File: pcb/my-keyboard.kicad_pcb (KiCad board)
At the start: 2 copper layers, 8 parts, among them J1 Conn_01x04_Socket, SW1 SW_Push, SW2 SW_Push, SW3 SW_Push, SW4 SW_Push, SW5 RotaryEncoder_Switch, SW6 RotaryEncoder_Switch, U1 MOUDLE-SEEEDUINO-XIAO

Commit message: New PCB and gerber files
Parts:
- added H1: MountingHole, MountingHole:MountingHole_3.5mm, F.Cu at (167.0, 98.5)
- added H2: MountingHole, MountingHole:MountingHole_3.5mm, F.Cu at (105.5, 65.0)
- added H3: MountingHole, MountingHole:MountingHole_3.5mm, F.Cu at (102.5, 104.0)
- moved SW5 0.56 mm to (161.0, 83.5)
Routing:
- net Net-(U1-PA11_A3_D3): track 53.3 -> 106.5 mm
- net Net-(U1-PA6_A10_D10_MOSI): track 45.4 -> 70.5 mm
- net Net-(U1-PA10_A2_D2): track 52.1 -> 33.1 mm
- net Net-(U1-PA7_A8_D8_SCK): track 93.2 -> 92.1 mm
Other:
- board outline added: 84.3 x 57.1 mm
- board text added: "Controller PCB by Antoni Borowski"

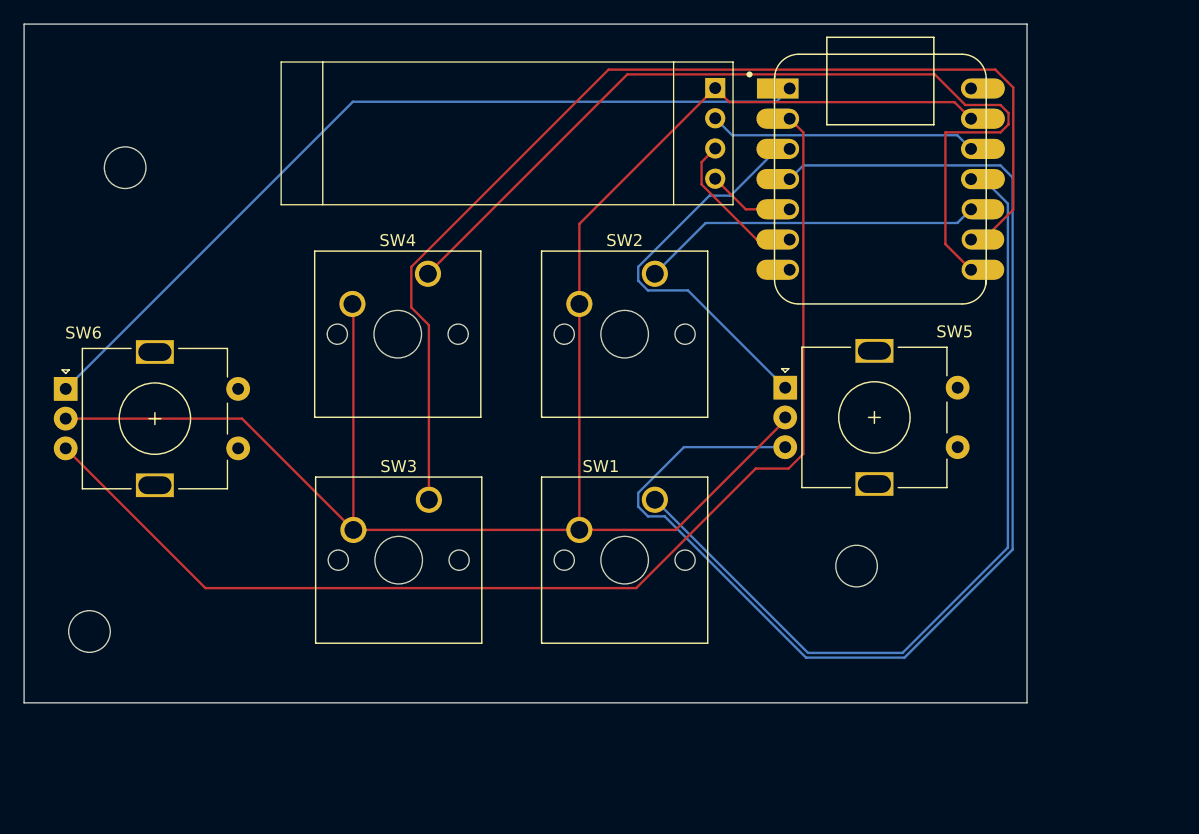
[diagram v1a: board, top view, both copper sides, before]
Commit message: Add diodes for keyboard matrix
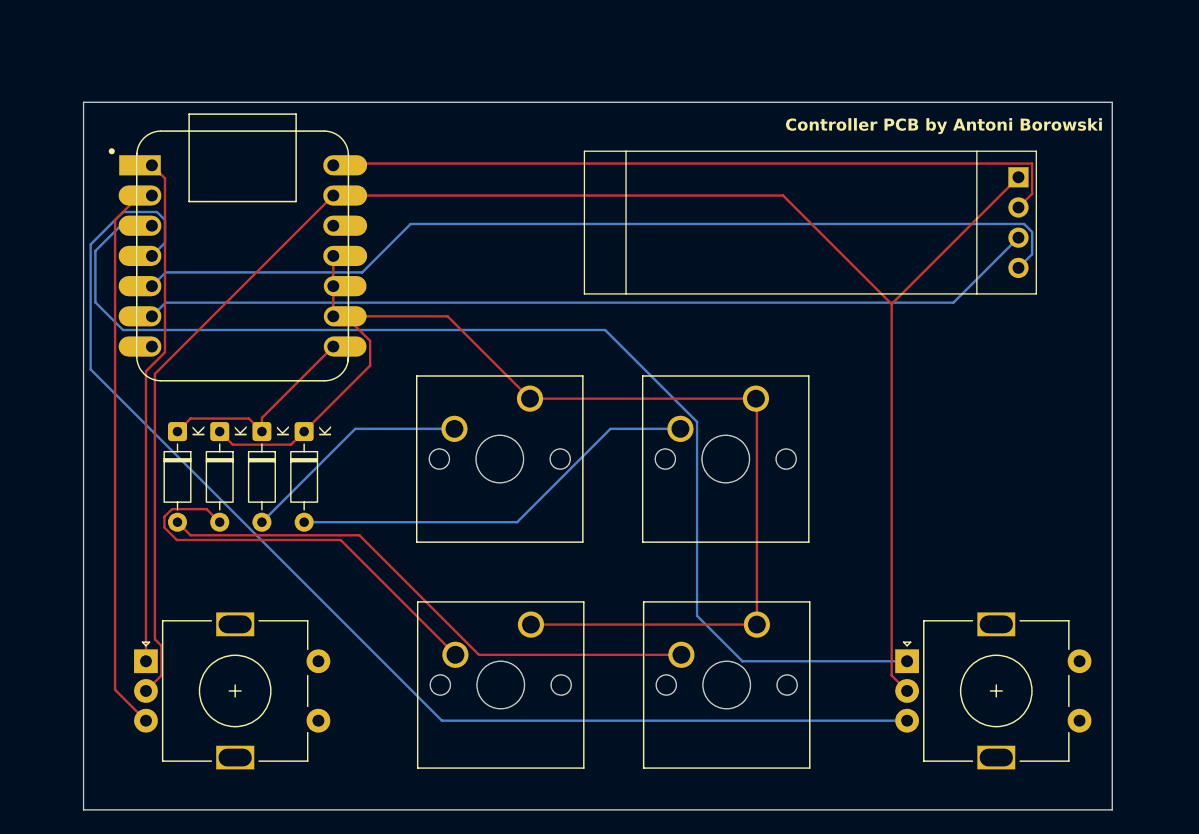
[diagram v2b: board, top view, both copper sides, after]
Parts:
- removed H1, H2, H3: MountingHole, MountingHole:MountingHole_3.5mm
- removed J1: Conn_01x04_Socket, footprints:SSD1306-0.91-OLED-4pin-128x32
- removed SW5, SW6: RotaryEncoder_Switch, Rotary_Encoder:RotaryEncoder_Alps_EC11E-Switch_Vertical_H20mm
- added D1: 1N4148, Diode_THT:D_DO-35_SOD27_P7.62mm_Horizontal, F.Cu at (120.5, 87.2)
- added D2: 1N4148, Diode_THT:D_DO-35_SOD27_P7.62mm_Horizontal, F.Cu at (117.0, 87.2)
- added D3: 1N4148, Diode_THT:D_DO-35_SOD27_P7.62mm_Horizontal, F.Cu at (113.5, 87.2)
- added D4: 1N4148, Diode_THT:D_DO-35_SOD27_P7.62mm_Horizontal, F.Cu at (109.9, 87.2)
- added J2: Conn_01x04, footprints:SSD1306-0.91-OLED-4pin-128x32, F.Cu at (144.1, 63.6)
- added SW7: RotaryEncoder_Switch, Rotary_Encoder:RotaryEncoder_Alps_EC11E-Switch_Vertical_H20mm, F.Cu at (107.2, 106.5)
- added SW8: RotaryEncoder_Switch, Rotary_Encoder:RotaryEncoder_Alps_EC11E-Switch_Vertical_H20mm, F.Cu at (171.2, 106.5)
- moved U1 54.0 mm to (115.4, 72.4)
- moved SW4 40.4 mm to (158.6, 103.4)
- moved SW2 14.8 mm to (139.5, 84.4)
- moved SW3 13.6 mm to (139.6, 103.4)
- moved SW1 12.0 mm to (158.5, 84.4)
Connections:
- SW1 pad 1: Net-(U1-PA6_A10_D10_MOSI) -> /COL0
- SW1 pad 2: GND -> Net-(D1-A)
- SW2 pad 1: Net-(U1-PA5_A9_D9_MISO) -> /COL0
- SW2 pad 2: GND -> Net-(D2-A)
- SW3 pad 1: Net-(U1-PA7_A8_D8_SCK) -> /COL0
- SW3 pad 2: GND -> Net-(D3-A)
- SW4 pad 1: Net-(U1-PB09_A7_D7_RX) -> /COL0
- SW4 pad 2: GND -> Net-(D4-A)
- U1 pad 1: Net-(U1-PA02_A0_D0) -> /REA1
- U1 pad 10: Net-(U1-PA5_A9_D9_MISO) -> /COL0
- U1 pad 11: Net-(U1-PA6_A10_D10_MOSI) -> /COL0
- U1 pad 12: Net-(J1-Pin_2) -> unconnected-(U1-3V3-Pad12)
- U1 pad 14: unconnected-(U1-5V-Pad14) -> +5V
- U1 pad 2: Net-(U1-PA4_A1_D1) -> /REB1
- U1 pad 3: Net-(U1-PA10_A2_D2) -> /REA2
- U1 pad 4: Net-(U1-PA11_A3_D3) -> /REB2
- U1 pad 5: Net-(J1-Pin_4) -> /SDA
- U1 pad 6: Net-(J1-Pin_3) -> /SCL
- U1 pad 8: Net-(U1-PB09_A7_D7_RX) -> /ROW1
- U1 pad 9: Net-(U1-PA7_A8_D8_SCK) -> /COL0
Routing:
- net Net-(U1-PA11_A3_D3): track 106.5 -> 0.00 mm
- net /REB2: track 0.00 -> 102.5 mm
- net /COL0: track 0.00 -> 102.3 mm
- net Net-(U1-PA4_A1_D1): track 100.2 -> 0.00 mm
- net /REA2: track 0.00 -> 97.6 mm
- net Net-(U1-PA7_A8_D8_SCK): track 92.1 -> 0.00 mm
- net /SDA: track 0.00 -> 80.0 mm
- net Net-(U1-PB09_A7_D7_RX): track 76.1 -> 0.00 mm
- net /SCL: track 0.00 -> 75.6 mm
- net Net-(U1-PA02_A0_D0): track 71.3 -> 0.00 mm
- net Net-(U1-PA6_A10_D10_MOSI): track 70.5 -> 0.00 mm
- net +5V: track 0.00 -> 62.8 mm
- net Net-(D4-A): track 0.00 -> 47.0 mm
- net /REB1: track 0.00 -> 46.1 mm
- net /REA1: track 0.00 -> 42.8 mm
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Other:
- board size 84.3 x 57.1 mm -> 86.5 x 59.5 mm
